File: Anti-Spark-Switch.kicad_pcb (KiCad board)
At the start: 2 copper layers, 63.2 x 42 mm, 16 parts, among them P1 Pad_Conn, P2 Pad_Conn, P3 Screw_Terminal, P4 Screw_Terminal, P5 Pad_Conn, P6 Pad_Conn, P7 CONN_01X02, Q1 IRFS7530, Q2 IRFS7530, Q3 IRFS7530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

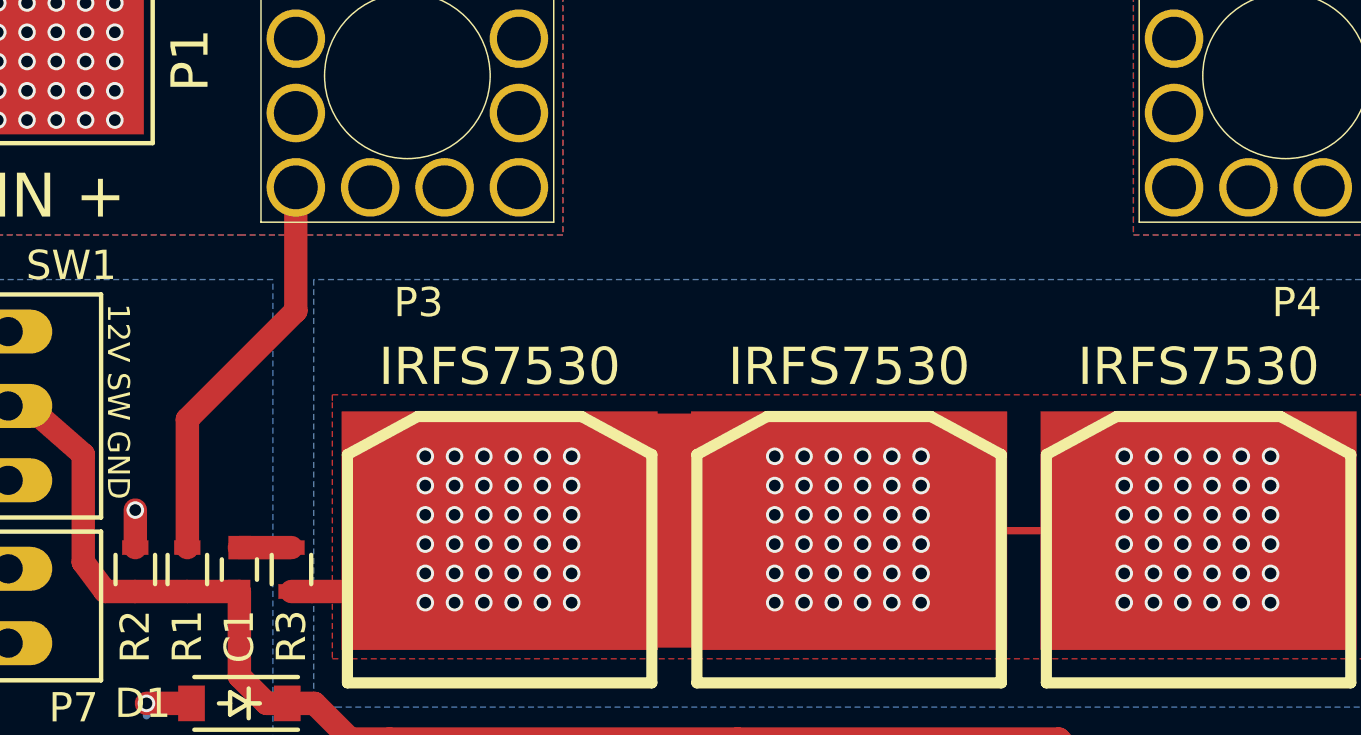
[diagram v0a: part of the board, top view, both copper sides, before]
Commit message: Rev 1.1 changes
Moved Gate power input from before to after fuse for improved safety
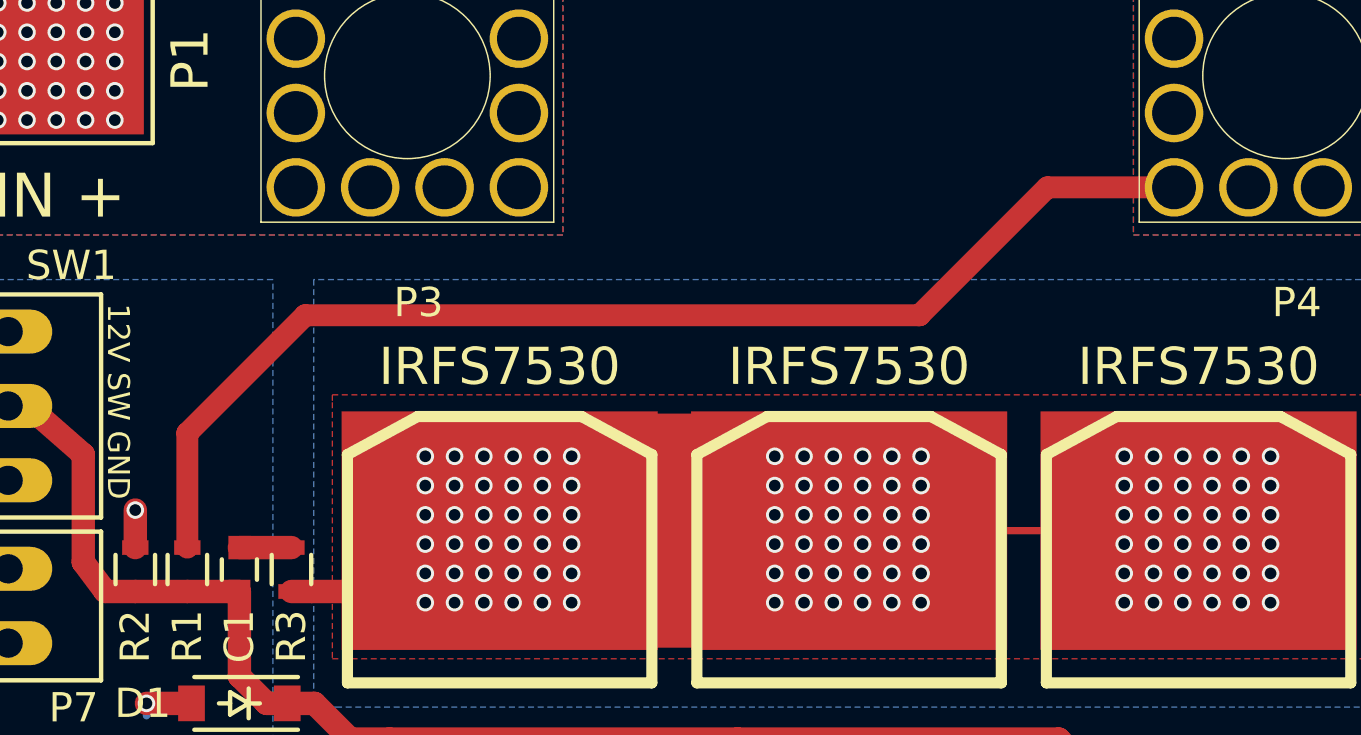
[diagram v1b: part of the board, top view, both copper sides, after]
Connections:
- R1 pad 1: VCC -> Net-(P4-Pad1)
- SW1 pad 3: +12V -> (no net)
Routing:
- net Net-(P4-Pad1): track 26.8 -> 67.9 mm
- net VCC: track 40.7 -> 26.8 mm
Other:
- board text added: "Ver: 1.1 Date: 9/16"
- board text removed: "Ver: 1.0 Date: 7/16"
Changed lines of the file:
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@@
 (kicad_pcb (version 4) (host pcbnew 4.0.2-stable)
   (general
-    (links 57)
+    (links 56)
     (no_connects 0)
     (area 179.924999 47.924999 243.325001 90.075001)
     (thickness 1.6)
     (drawings 14)
-    (tracks 677)
+    (tracks 679)
     (zones 0)
     (modules 16)
@@
     (pad 2 thru_hole oval (at 0 0 90) (size 1.50622 3.01498) (drill 0.99822) (layers *.Cu *.Mask)
       (net 3 "Net-(C1-Pad2)"))
-    (pad 3 thru_hole oval (at 2.54 0 90) (size 1.50622 3.01498) (drill 0.99822) (layers *.Cu *.Mask)
-      (net 7 +12V))
+    (pad 3 thru_hole oval (at 2.54 0 90) (size 1.50622 3.01498) (drill 0.99822) (layers *.Cu *.Mask))
   )
   (module Capacitors_SMD:C_0603 (layer F.Cu)
@@
     (fp_line (start -0.5 -0.675) (end 0.5 -0.675) (layer F.SilkS) (width 0.15))
     (pad 1 smd rect (at -0.75 0 270) (size 0.5 0.9) (layers F.Cu F.Paste F.Mask)
-      (net 1 VCC))
+      (net 5 "Net-(P4-Pad1)"))
     (pad 2 smd rect (at 0.75 0 270) (size 0.5 0.9) (layers F.Cu F.Paste F.Mask)
       (net 3 "Net-(C1-Pad2)"))
@@
     (effects (font (size 0.75 0.75) (thickness 0.1875)))
   )
-  (gr_text "Ver: 1.0\nDate: 7/16" (at 212.344 54.4322) (layer B.SilkS)
+  (gr_text "Ver: 1.1\nDate: 9/16" (at 212.344 54.4322) (layer B.SilkS)
     (effects (font (size 1.5 1.5) (thickness 0.3)) (justify mirror))
   )
@@
   (gr_line (start 180 90) (end 243.25 90) (angle 90) (layer Edge.Cuts) (width 0.15))
   (gr_line (start 180 48) (end 180 90) (angle 90) (layer Edge.Cuts) (width 0.15))
-  (segment (start 193.19 57.81) (end 193.19 62.0292) (width 0.8) (layer F.Cu) (net 1))
-  (segment (start 189.484 65.7352) (end 189.484 70.116) (width 0.8) (layer F.Cu) (net 1))
-  (segment (start 193.19 62.0292) (end 189.484 65.7352) (width 0.8) (layer F.Cu) (net 1))
   (segment (start 186.007 55.5112) (end 187.007 55.5112) (width 0.25) (layer F.Cu) (net 1))
   (segment (start 185.007 55.5112) (end 186.007 55.5112) (width 0.25) (layer F.Cu) (net 1))
@@
   (segment (start 191.262 71.616) (end 189.484 71.616) (width 0.8) (layer F.Cu) (net 3))
   (segment (start 193.04 70.116) (end 191.262 70.116) (width 0.8) (layer F.Cu) (net 4))
+  (segment (start 193.51 62.18) (end 189.484 66.206) (width 0.75) (layer F.Cu) (net 5))
+  (segment (start 189.484 66.206) (end 189.484 70.116) (width 0.75) (layer F.Cu) (net 5))
+  (segment (start 214.495787 62.18) (end 193.51 62.18) (width 0.75) (layer F.Cu) (net 5))
+  (segment (start 223.19 57.81) (end 218.865787 57.81) (width 0.75) (layer F.Cu) (net 5) (status 400000))
+  (segment (start 218.865787 57.81) (end 214.495787 62.18) (width 0.75) (layer F.Cu) (net 5))
   (segment (start 238.0074 55.4858) (end 237.0074 55.4858) (width 0.25) (layer F.Cu) (net 5))
   (segment (start 239.0074 55.4858) (end 238.0074 55.4858) (width 0.25) (layer F.Cu) (net 5))

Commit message: minor Rev 1.1 changes
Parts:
- C1: footprint Capacitors_SMD:C_0603 -> Capacitors_SMD:C_0603_HandSoldering
- P1, P2, P5, P6: footprint sparkparts:1PAD_6x5mm -> Spark_Parts:1PAD_8x7mm
- R1, R2, R3: footprint Resistors_SMD:R_0603 -> Resistors_SMD:R_0603_HandSoldering
- moved P1 0.52 mm to (185.5, 53.5)
- moved P5 0.49 mm to (238.5, 53.5)
- moved P6 0.40 mm to (238.6, 85.7)
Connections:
- SW1 pad 3: (no net) -> +12V
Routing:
- net +12V: track 13.9 -> 14.7 mm
- net Net-(C1-Pad2): track 55.6 -> 56.1 mm

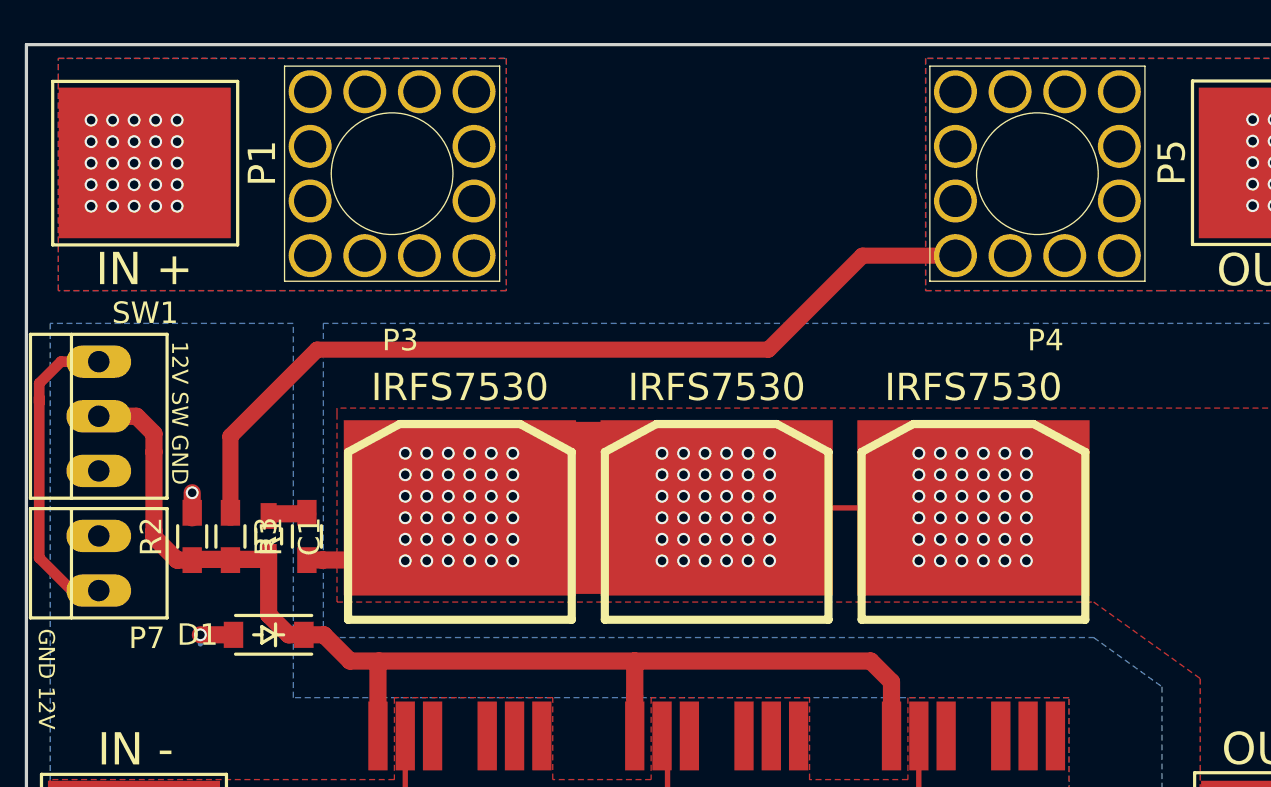
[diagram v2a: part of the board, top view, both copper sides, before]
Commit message: updated a footprint, fixed reference numbers
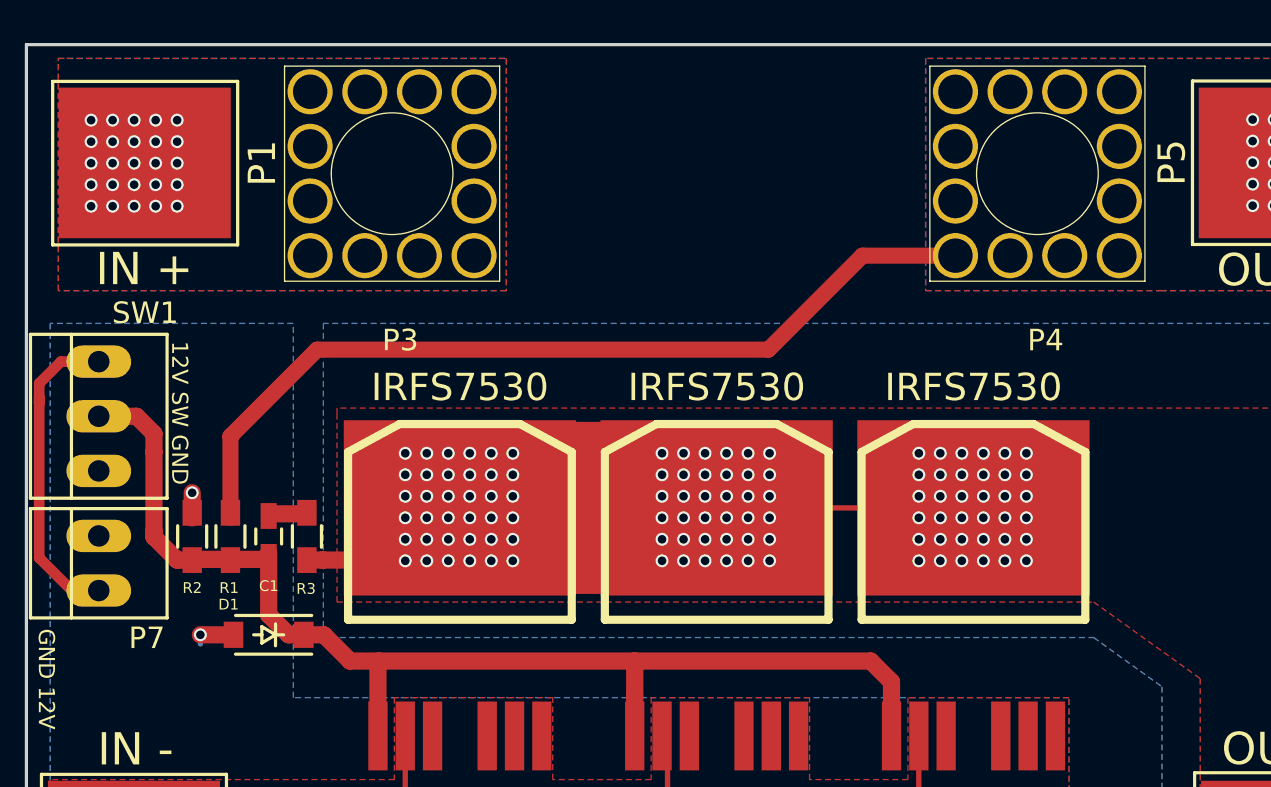
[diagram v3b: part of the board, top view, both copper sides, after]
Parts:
- P3, P4: footprint sparkparts:M5_Screw_Terminal_12_pin -> Spark_Parts:M5_Screw_Terminal_12_pin
